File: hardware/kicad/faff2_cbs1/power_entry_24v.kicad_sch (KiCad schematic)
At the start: 0 parts

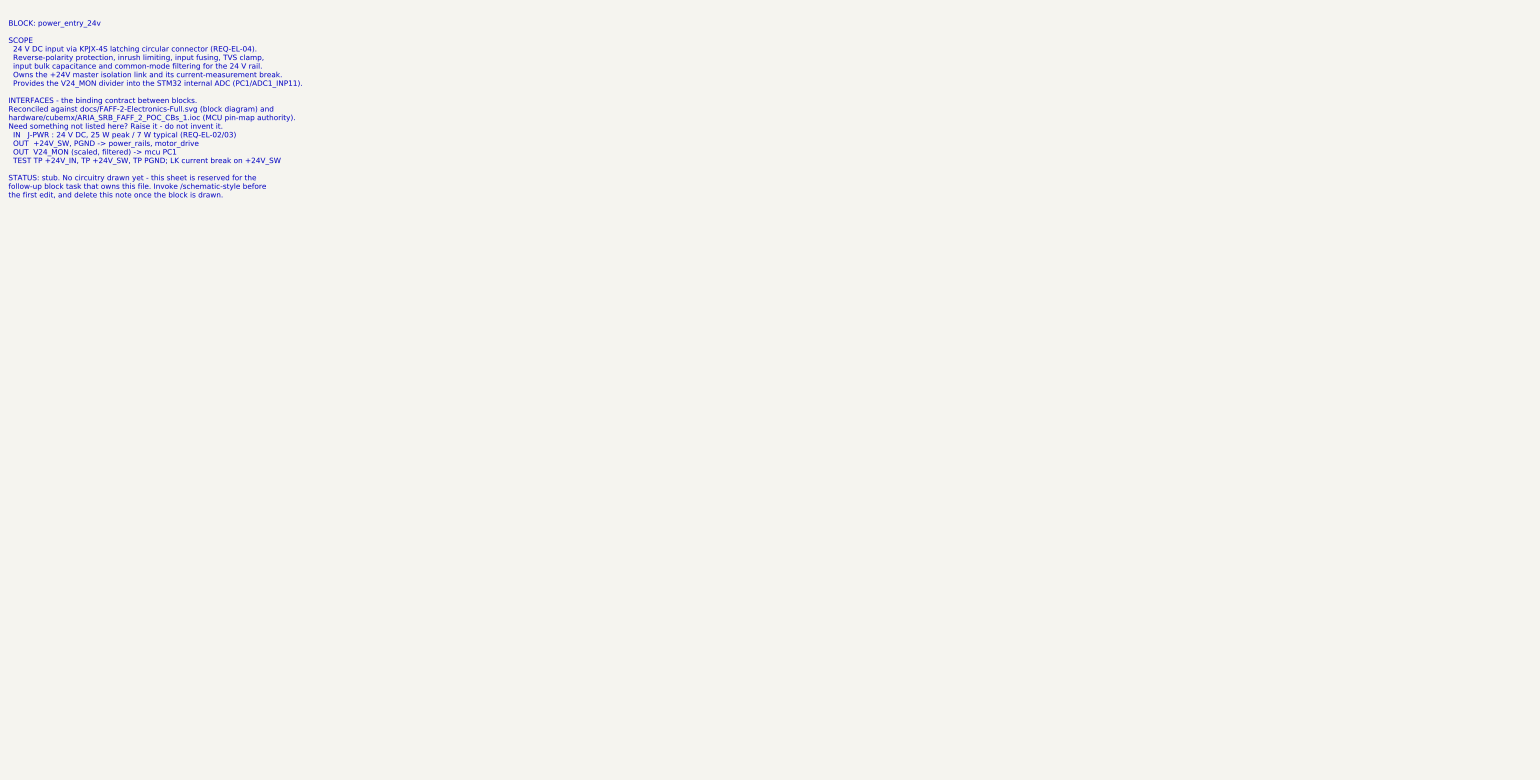
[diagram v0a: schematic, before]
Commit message: power: draw the 24 V entry and rail blocks
power_entry_24v: KPJX-4S 24 V in with doubled contacts, 2 A time-lag fuse,
common-mode choke on both lines, P-channel reverse-polarity series FET with a
gate-source soft start, 5 kW TVS and bulk downstream of it, and the V24_MON
divider into PC1. Two independent 0R branch links so the motor stage can be
left unpowered while the rest of the board is brought up (TEST_PLAN 3.3).

power_rails: answers OQ-02 and OQ-07. LMR33630 buck to a 5.5 V pre-regulator
feeding two TPS7A20 LDOs (+5V digital for the IKP11 read head, +5VA analog for
the ADCs and the AFE excitation chain), a second LMR33630 buck to +3V3, and a
ferrite-isolated +3V3A for the ADC digital supplies. Per-rail isolation link /
current break / test point, a feedback test point per converter, a shared
16.2 V EN divider for undervoltage lockout, and RAIL_PGOOD as the wired-AND of
both converters' power-good flags.

Designators follow the AGENTS.md range scheme: power_entry_24v 2xx,
power_rails 3xx. This block owns the single PWR_FLAG for GND, +24V_SW,
V24_LOGIC, +5V5, +5V, +5VA, +3V3 and +3V3A, which clears the
power_pin_not_driven class AGENTS.md flags as pending on power_rails.

ERC at --severity-all: these sheets contribute 0 warnings and 5 errors, all
hier_label_mismatch from the deliberately unwired root sheet (DEC-0009) and
cleared by the integration pass. Overlap checker clean across the project;
orientation-sensitive parts verified from the netlist, not by eye.

Reasoning, the root sheet's sheet-pin list and the residual ERC are in
docs/decisions/actuator-sch-power.md.

Co-Authored-By: Claude Opus 5 <noreply@anthropic.com>
Claude-Session: https://claude.ai/code/session_01K6s18nKQUV4o9kutpLBscJ
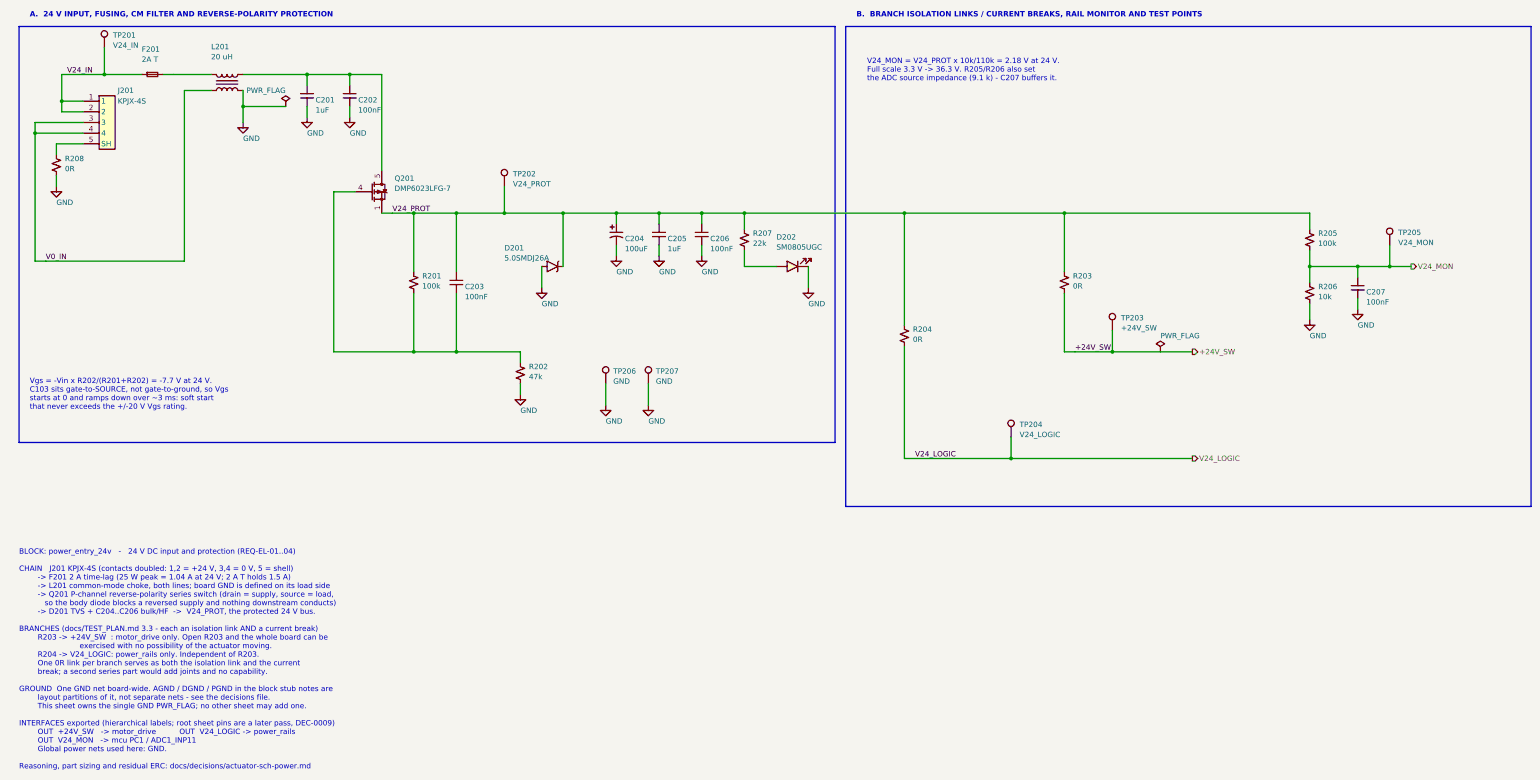
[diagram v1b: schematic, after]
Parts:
- added C201, C205: 1uF, Amodo:C_0805_2012Metric, symbol Amodo_Capacitors:CAP_MLCC_1uF_0805_10%_100V
- added C202, C206: 100nF, Amodo:C_0805_2012Metric, symbol Amodo_Capacitors:CAP_MLCC_100nF_0805_10%_100V
- added C203, C207: 100nF, Amodo:C_0603_1608Metric, symbol Amodo_Capacitors:CAP_MLCC_100nF_0603_20%_50V
- added C204: 100uF, Amodo:C_ALU_D10_L10.2_SMT_ANTI-VIBE, symbol Amodo_Capacitors:CAP_ALU_100UF_SMD_20%_63V
- added D201: 5.0SMDJ26A, Amodo:DO-214AB, symbol Amodo_Diodes:5.0SMDJ26A
- added D202: SM0805UGC, Amodo:LED 0805 SM0805, symbol Amodo_LEDs:LED_SMD_0805_GREEN
- added F201: 2A T, Amodo:FUSE_157T_LittelFuse, symbol Amodo_Fuses:FUSE_2A_T_125V_SMT_REPLACEABLE
- added J201: KPJX-4S, Amodo:KPJX-4S, symbol Amodo_Connectors:KYCON_KPJX_4S
- added L201: 20 uH, Amodo:PLT10HH101150PN#, symbol Amodo_Inductors:PLT10HH1026R0PN#
- added Q201: DMP6023LFG-7, Amodo:DMP4013LFG7, symbol Amodo_Power_Transistors:DMP6023LFG-7
- added R201, R205: 100k, Amodo:R_0603_1608Metric, symbol Amodo_Resistors:RES_TF_100k_0603
- added R202: 47k, Amodo:R_0603_1608Metric, symbol Amodo_Resistors:RES_TF_47k_0603
- added R203, R204: 0R, Amodo:R_1206_3216Metric, symbol Amodo_Resistors:RES_TF_0R_1206_10A
- added R206: 10k, Amodo:R_0603_1608Metric, symbol Amodo_Resistors:RES_TF_10k_0603
- added R207: 22k, Amodo:R_0603_1608Metric, symbol Amodo_Resistors:RES_TF_22k_0603
- added R208: 0R, Amodo:R_0603_1608Metric, symbol Amodo_Resistors:RES_TF_0R_0603
- added TP201: V24_IN, Amodo:KeystoneMiniatureTestLoop, symbol Amodo_Connectors:TestPointHook
- added TP202: V24_PROT, Amodo:KeystoneMiniatureTestLoop, symbol Amodo_Connectors:TestPointHook
- added TP203: +24V_SW, Amodo:KeystoneMiniatureTestLoop, symbol Amodo_Connectors:TestPointHook
- added TP204: V24_LOGIC, Amodo:KeystoneMiniatureTestLoop, symbol Amodo_Connectors:TestPointHook
- added TP205: V24_MON, Amodo:TestPoint_Pad_D1.0mm, symbol Amodo_Connectors:TestPoint
- added TP206, TP207: GND, Amodo:KeystoneMiniatureTestLoop, symbol Amodo_Connectors:TestPointHook
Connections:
- new net: C201.1, C202.1, L201.2, Q201.5 (D)
- new net: D202.1, R207.2
- new net: C203.2, Q201.4 (G), R201.2, R202.1
- new net: J201.5 (SH), R208.1
- new net: F201.2, L201.1
- new net +24V_SW: R203.2, TP203.1
- new net GND: C201.2, C202.2, C204.2, C205.2, C206.2, C207.2, D201.1 (A1), D202.2, L201.3, R202.2, R206.2, R208.2, TP206.1, TP207.1
- new net V0_IN: J201.3, J201.4, L201.4
- new net V24_IN: F201.1, J201.1, J201.2, TP201.1
- new net V24_LOGIC: R204.2, TP204.1
- new net V24_MON: C207.1, R205.2, R206.1, TP205.1
- new net V24_PROT: C203.1, C204.1, C205.1, C206.1, D201.2 (A2), Q201.1 (S), R201.1, R203.1, R204.1, R205.1, R207.1, TP202.1
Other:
- note added: "A. 24 V INPUT, FUSING, CM FILTER AND REVERSE-POLARITY PROTECTION"
- note added: "B. BRANCH ISOLATION LINKS / CURRENT BREAKS, RAIL MONITOR AND TEST POINTS"
- note added: "BLOCK: power_entry_24v - 24 V DC input and protection (REQ-EL-01..04) CHAIN J201 KPJX-4S (contacts doubled: 1,2 = +24 V, 3,4 = 0 V, 5 = shell) -> F201 2 A time-lag (25 W peak = 1.04 A at 24 V; 2 A T holds 1.5 A) -> L201 common-mode choke, both lines; board GND is defined on its load side -> Q201 P-channel reverse-polarity series switch (drain = supply, source = load, so the body diode blocks a re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"
- note added: "V24_MON = V24_PROT x 10k/110k = 2.18 V at 24 V. Full scale 3.3 V -> 36.3 V. R205/R206 also set the ADC source impedance (9.1 k) - C207 buffers it."
- note added: "Vgs = -Vin x R202/(R201+R202) = -7.7 V at 24 V. C103 sits gate-to-SOURCE, not gate-to-ground, so Vgs starts at 0 and ramps down over ~3 ms: soft start that never exceeds the +/-20 V Vgs rating."
- note removed: "BLOCK: power_entry_24v SCOPE 24 V DC input via KPJX-4S latching circular connector (REQ-EL-04). Reverse-polarity protection, inrush limiting, input fusing, TVS clamp, input bulk capacitance and common-mode filtering for the 24 V rail. Owns the +24V master isolation link and its current-measurement break. Provides the V24_MON divider into the STM32 internal ADC (PC1/ADC1_INP11). INTERFACES - the b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"
